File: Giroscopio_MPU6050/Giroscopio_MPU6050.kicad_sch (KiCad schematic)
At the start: 6 parts, among them U301 MPU-6050

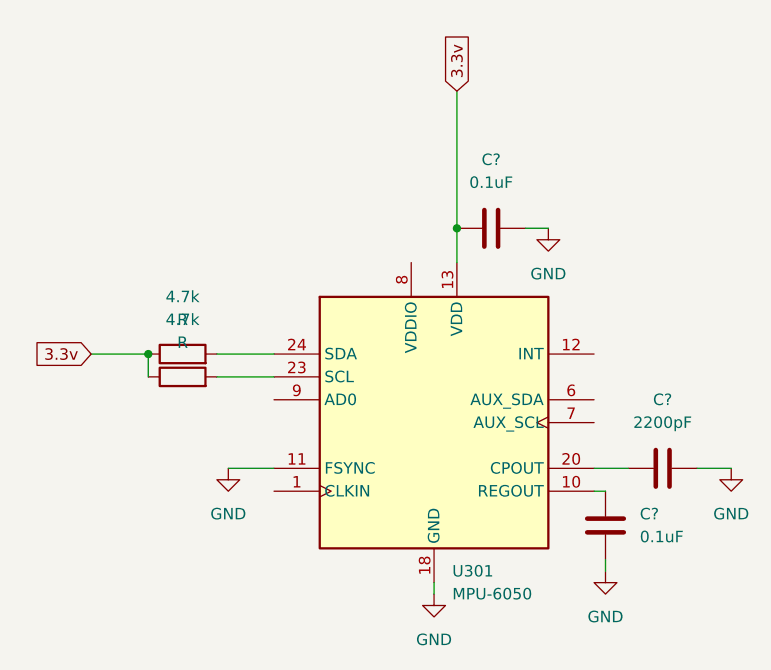
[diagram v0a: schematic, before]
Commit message: MPU6050: Anotazione da 400
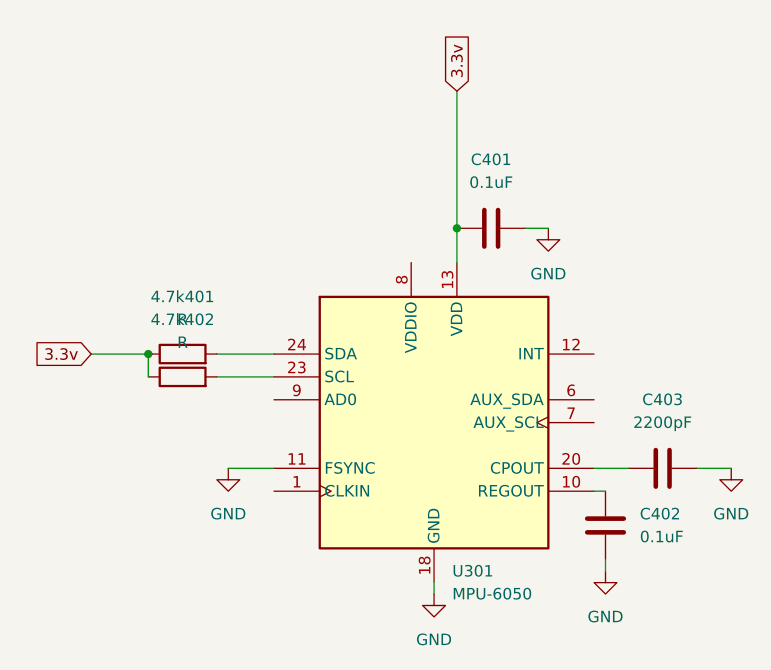
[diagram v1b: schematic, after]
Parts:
- gave numbers to parts that had none: 3
- renumbered 4.7k to 4.7k401, 4.7k to 4.7k402
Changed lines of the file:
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@@
   (symbol (lib_id "Device:R") (at 110.49 76.2 90) (unit 1)
     (in_bom yes) (on_board yes) (fields_autoplaced)
-    (property "Reference" "4.7k" (id 0) (at 110.49 69.85 90))
+    (property "Reference" "4.7k401" (id 0) (at 110.49 69.85 90))
     (property "Value" "R" (id 1) (at 110.49 72.39 90))
     (property "Footprint" "" (id 2) (at 110.49 77.978 90)
@@
   (symbol (lib_id "power:GND") (at 115.57 88.9 0) (unit 1)
     (in_bom yes) (on_board yes) (fields_autoplaced)
-    (property "Reference" "#PWR?" (id 0) (at 115.57 95.25 0)
+    (property "Reference" "#PWR0104" (id 0) (at 115.57 95.25 0)
       (effects (font (size 1.27 1.27)) hide)
     )
@@
   (symbol (lib_id "Device:R") (at 110.49 78.74 90) (unit 1)
     (in_bom yes) (on_board yes) (fields_autoplaced)
-    (property "Reference" "4.7k" (id 0) (at 110.49 72.39 90))
+    (property "Reference" "4.7k402" (id 0) (at 110.49 72.39 90))
     (property "Value" "R" (id 1) (at 110.49 74.93 90))
     (property "Footprint" "" (id 2) (at 110.49 80.518 90)
@@
   (symbol (lib_id "power:GND") (at 151.13 62.23 0) (unit 1)
     (in_bom yes) (on_board yes) (fields_autoplaced)
-    (property "Reference" "#PWR?" (id 0) (at 151.13 68.58 0)
+    (property "Reference" "#PWR0105" (id 0) (at 151.13 68.58 0)
       (effects (font (size 1.27 1.27)) hide)
     )
@@
   (symbol (lib_id "Device:C") (at 163.83 88.9 90) (unit 1)
     (in_bom yes) (on_board yes) (fields_autoplaced)
-    (property "Reference" "C?" (id 0) (at 163.83 81.28 90))
+    (property "Reference" "C403" (id 0) (at 163.83 81.28 90))
     (property "Value" "2200pF" (id 1) (at 163.83 83.82 90))
     (property "Footprint" "" (id 2) (at 167.64 87.9348 0)
@@
   (symbol (lib_id "power:GND") (at 171.45 88.9 0) (unit 1)
     (in_bom yes) (on_board yes) (fields_autoplaced)
-    (property "Reference" "#PWR?" (id 0) (at 171.45 95.25 0)
+    (property "Reference" "#PWR0101" (id 0) (at 171.45 95.25 0)
       (effects (font (size 1.27 1.27)) hide)
     )
@@
   (symbol (lib_id "power:GND") (at 138.43 102.87 0) (unit 1)
     (in_bom yes) (on_board yes) (fields_autoplaced)
-    (property "Reference" "#PWR?" (id 0) (at 138.43 109.22 0)
+    (property "Reference" "#PWR0103" (id 0) (at 138.43 109.22 0)
       (effects (font (size 1.27 1.27)) hide)
     )
@@
   (symbol (lib_id "Device:C") (at 157.48 95.25 0) (unit 1)
     (in_bom yes) (on_board yes) (fields_autoplaced)
-    (property "Reference" "C?" (id 0) (at 161.29 93.9799 0)
+    (property "Reference" "C402" (id 0) (at 161.29 93.9799 0)
       (effects (font (size 1.27 1.27)) (justify left))
     )
@@
   (symbol (lib_id "Device:C") (at 144.78 62.23 90) (unit 1)
     (in_bom yes) (on_board yes) (fields_autoplaced)
-    (property "Reference" "C?" (id 0) (at 144.78 54.61 90))
+    (property "Reference" "C401" (id 0) (at 144.78 54.61 90))
     (property "Value" "0.1uF" (id 1) (at 144.78 57.15 90))
     (property "Footprint" "" (id 2) (at 148.59 61.2648 0)
@@
   (symbol (lib_id "power:GND") (at 157.48 100.33 0) (unit 1)
     (in_bom yes) (on_board yes) (fields_autoplaced)
-    (property "Reference" "#PWR?" (id 0) (at 157.48 106.68 0)
+    (property "Reference" "#PWR0102" (id 0) (at 157.48 106.68 0)
       (effects (font (size 1.27 1.27)) hide)
     )
@@
   )
   (symbol_instances
+    (path "/7f7c15d3-18ea-4956-9bc9-333dcb868788"
+      (reference "#PWR0101") (unit 1) (value "GND") (footprint "")
+    )
+    (path "/f2b7ad6b-a0fd-4064-8d62-fde73296124e"
+      (reference "#PWR0102") (unit 1) (value "GND") (footprint "")
+    )
+    (path "/99e08e2b-8918-43dc-a1ad-dcdcb898f573"
+      (reference "#PWR0103") (unit 1) (value "GND") (footprint "")
+    )
     (path "/50316e17-b33b-437a-94a0-2744829286a7"
-      (reference "#PWR?") (unit 1) (value "GND") (footprint "")
+      (reference "#PWR0104") (unit 1) (value "GND") (footprint "")
     )
     (path "/589326c2-ec44-4412-bc73-b09a8f665eaf"
-      (reference "#PWR?") (unit 1) (value "GND") (footprint "")
-    )
-    (path "/7f7c15d3-18ea-4956-9bc9-333dcb868788"
-      (reference "#PWR?") (unit 1) (value "GND") (footprint "")
-    )
-    (path "/99e08e2b-8918-43dc-a1ad-dcdcb898f573"
-      (reference "#PWR?") (unit 1) (value "GND") (footprint "")
-    )
-    (path "/f2b7ad6b-a0fd-4064-8d62-fde73296124e"
-      (reference "#PWR?") (unit 1) (value "GND") (footprint "")
+      (reference "#PWR0105") (unit 1) (value "GND") (footprint "")
     )
     (path "/2e251504-40fb-405f-85d7-132692c512d3"
-      (reference "4.7k") (unit 1) (value "R") (footprint "")
+      (reference "4.7k401") (unit 1) (value "R") (footprint "")
     )
     (path "/55873c7a-b6a3-4c95-8d35-5ea9c6f0e1e7"
-      (reference "4.7k") (unit 1) (value "R") (footprint "")
+      (reference "4.7k402") (unit 1) (value "R") (footprint "")
+    )
+    (path "/a2eb4743-8fae-4769-891d-2e9efdac6042"
+      (reference "C401") (unit 1) (value "0.1uF") (footprint "")
+    )
+    (path "/9b047bc1-0203-4b51-9939-6f7c5b0d22c4"
+      (reference "C402") (unit 1) (value "0.1uF") (footprint "")
     )
     (path "/719e2d86-e50e-4472-aa02-ffcb840f9afa"
-      (reference "C?") (unit 1) (value "2200pF") (footprint "")
-    )
-    (path "/9b047bc1-0203-4b51-9939-6f7c5b0d22c4"
-      (reference "C?") (unit 1) (value "0.1uF") (footprint "")
-    )
-    (path "/a2eb4743-8fae-4769-891d-2e9efdac6042"
-      (reference "C?") (unit 1) (value "0.1uF") (footprint "")
+      (reference "C403") (unit 1) (value "2200pF") (footprint "")
     )
     (path "/da7199a3-f536-4f53-8142-9e41548cc6d8"
